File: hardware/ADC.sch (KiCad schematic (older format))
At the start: 21 parts, among them J4 691327310016, J5 691327310016

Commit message: Assigning footprints
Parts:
- C33, C34, C35, C36, C37, C38, C39, C40, C41, C42, C43, C44, C45, C46, C47, C48, C49, C50: renamed from C?; footprint (none) -> Capacitor_SMD:C_0603_1608Metric
- U1: renamed from U?; footprint QFP50P1200X1200X160-64N -> ADS8556IPM:QFP50P1200X1200X160-64N
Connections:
- net AVDD renamed 5V
- net BVDD renamed 3V3
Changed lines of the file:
@@
 AGND
 $Comp
-L antena:C C?
+L antena:C C33
 U 1 1 5E30FC12
 P 850 1150
-F 0 "C?" H 965 1196 50  0000 L CNN
+F 0 "C33" H 965 1196 50  0000 L CNN
 F 1 "100n" H 965 1105 50  0000 L CNN
-F 2 "" H 888 1000 50  0001 C CNN
+F 2 "Capacitor_SMD:C_0603_1608Metric" H 888 1000 50  0001 C CNN
 F 3 "~" H 850 1150 50  0001 C CNN
 	1    850  1150
@@
 AGND
 $Comp
-L antena:C C?
+L antena:C C38
 U 1 1 5E310EB0
 P 1300 1150
-F 0 "C?" H 1415 1196 50  0000 L CNN
+F 0 "C38" H 1415 1196 50  0000 L CNN
 F 1 "100n" H 1415 1105 50  0000 L CNN
-F 2 "" H 1338 1000 50  0001 C CNN
+F 2 "Capacitor_SMD:C_0603_1608Metric" H 1338 1000 50  0001 C CNN
 F 3 "~" H 1300 1150 50  0001 C CNN
 	1    1300 1150
@@
 AGND
 $Comp
-L antena:C C?
+L antena:C C41
 U 1 1 5E311894
 P 1700 1150
-F 0 "C?" H 1815 1196 50  0000 L CNN
+F 0 "C41" H 1815 1196 50  0000 L CNN
 F 1 "100n" H 1815 1105 50  0000 L CNN
-F 2 "" H 1738 1000 50  0001 C CNN
+F 2 "Capacitor_SMD:C_0603_1608Metric" H 1738 1000 50  0001 C CNN
 F 3 "~" H 1700 1150 50  0001 C CNN
 	1    1700 1150
@@
 AGND
 $Comp
-L antena:C C?
+L antena:C C46
 U 1 1 5E31189E
 P 2150 1150
-F 0 "C?" H 2265 1196 50  0000 L CNN
+F 0 "C46" H 2265 1196 50  0000 L CNN
 F 1 "100n" H 2265 1105 50  0000 L CNN
-F 2 "" H 2188 1000 50  0001 C CNN
+F 2 "Capacitor_SMD:C_0603_1608Metric" H 2188 1000 50  0001 C CNN
 F 3 "~" H 2150 1150 50  0001 C CNN
 	1    2150 1150
@@
 AGND
 $Comp
-L antena:C C?
+L antena:C C34
 U 1 1 5E3124A7
 P 850 2250
-F 0 "C?" H 965 2296 50  0000 L CNN
+F 0 "C34" H 965 2296 50  0000 L CNN
 F 1 "100n" H 965 2205 50  0000 L CNN
-F 2 "" H 888 2100 50  0001 C CNN
+F 2 "Capacitor_SMD:C_0603_1608Metric" H 888 2100 50  0001 C CNN
 F 3 "~" H 850 2250 50  0001 C CNN
 	1    850  2250
@@
 AGND
 $Comp
-L antena:C C?
+L antena:C C39
 U 1 1 5E3124B1
 P 1300 2250
-F 0 "C?" H 1415 2296 50  0000 L CNN
+F 0 "C39" H 1415 2296 50  0000 L CNN
 F 1 "100n" H 1415 2205 50  0000 L CNN
-F 2 "" H 1338 2100 50  0001 C CNN
+F 2 "Capacitor_SMD:C_0603_1608Metric" H 1338 2100 50  0001 C CNN
 F 3 "~" H 1300 2250 50  0001 C CNN
 	1    1300 2250
@@
 AGND
 $Comp
-L antena:C C?
+L antena:C C42
 U 1 1 5E3124BB
 P 1700 2250
-F 0 "C?" H 1815 2296 50  0000 L CNN
+F 0 "C42" H 1815 2296 50  0000 L CNN
 F 1 "100n" H 1815 2205 50  0000 L CNN
-F 2 "" H 1738 2100 50  0001 C CNN
+F 2 "Capacitor_SMD:C_0603_1608Metric" H 1738 2100 50  0001 C CNN
 F 3 "~" H 1700 2250 50  0001 C CNN
 	1    1700 2250
@@
 AGND
 $Comp
-L antena:C C?
+L antena:C C47
 U 1 1 5E3124C5
 P 2150 2250
-F 0 "C?" H 2265 2296 50  0000 L CNN
+F 0 "C47" H 2265 2296 50  0000 L CNN
 F 1 "100n" H 2265 2205 50  0000 L CNN
-F 2 "" H 2188 2100 50  0001 C CNN
+F 2 "Capacitor_SMD:C_0603_1608Metric" H 2188 2100 50  0001 C CNN
 F 3 "~" H 2150 2250 50  0001 C CNN
 	1    2150 2250
@@
 AGND
 $Comp
-L antena:C C?
+L antena:C C35
 U 1 1 5E31354C
 P 850 3450
-F 0 "C?" H 965 3496 50  0000 L CNN
+F 0 "C35" H 965 3496 50  0000 L CNN
 F 1 "100n" H 965 3405 50  0000 L CNN
-F 2 "" H 888 3300 50  0001 C CNN
+F 2 "Capacitor_SMD:C_0603_1608Metric" H 888 3300 50  0001 C CNN
 F 3 "~" H 850 3450 50  0001 C CNN
 	1    850  3450
@@
 	850  3600 850  3750
 $Comp
-L antena:C C?
+L antena:C C49
 U 1 1 5E315C6D
 P 7900 2450
-F 0 "C?" V 8152 2450 50  0000 C CNN
+F 0 "C49" V 8152 2450 50  0000 C CNN
 F 1 "10uF" V 8061 2450 50  0000 C CNN
-F 2 "" H 7938 2300 50  0001 C CNN
+F 2 "Capacitor_SMD:C_0603_1608Metric" H 7938 2300 50  0001 C CNN
 F 3 "~" H 7900 2450 50  0001 C CNN
 	1    7900 2450
@@
 $EndComp
 $Comp
-L antena:C C?
+L antena:C C50
 U 1 1 5E315D24
 P 7900 3750
-F 0 "C?" V 8152 3750 50  0000 C CNN
+F 0 "C50" V 8152 3750 50  0000 C CNN
 F 1 "10uF" V 8061 3750 50  0000 C CNN
-F 2 "" H 7938 3600 50  0001 C CNN
+F 2 "Capacitor_SMD:C_0603_1608Metric" H 7938 3600 50  0001 C CNN
 F 3 "~" H 7900 3750 50  0001 C CNN
 	1    7900 3750
@@
 $EndComp
 $Comp
-L antena:C C?
+L antena:C C48
 U 1 1 5E315E2D
 P 7600 3650
-F 0 "C?" V 7852 3650 50  0000 C CNN
+F 0 "C48" V 7852 3650 50  0000 C CNN
 F 1 "10uF" V 7761 3650 50  0000 C CNN
-F 2 "" H 7638 3500 50  0001 C CNN
+F 2 "Capacitor_SMD:C_0603_1608Metric" H 7638 3500 50  0001 C CNN
 F 3 "~" H 7600 3650 50  0001 C CNN
 	1    7600 3650
@@
 AGND
 $Comp
-L antena:C C?
+L antena:C C40
 U 1 1 5E31DDD7
 P 1300 3450
-F 0 "C?" H 1415 3496 50  0000 L CNN
+F 0 "C40" H 1415 3496 50  0000 L CNN
 F 1 "470n" H 1415 3405 50  0000 L CNN
-F 2 "" H 1338 3300 50  0001 C CNN
+F 2 "Capacitor_SMD:C_0603_1608Metric" H 1338 3300 50  0001 C CNN
 F 3 "~" H 1300 3450 50  0001 C CNN
 	1    1300 3450
@@
 AGND
 $Comp
-L antena:C C?
+L antena:C C44
 U 1 1 5E31FB8F
 P 1800 3450
-F 0 "C?" H 1915 3496 50  0000 L CNN
+F 0 "C44" H 1915 3496 50  0000 L CNN
 F 1 "1uF" H 1915 3405 50  0000 L CNN
-F 2 "" H 1838 3300 50  0001 C CNN
+F 2 "Capacitor_SMD:C_0603_1608Metric" H 1838 3300 50  0001 C CNN
 F 3 "~" H 1800 3450 50  0001 C CNN
 	1    1800 3450
@@
 	7950 5050 8100 5050
 $Comp
-L antena:C C?
+L antena:C C37
 U 1 1 5E327225
 P 1250 4800
-F 0 "C?" H 1365 4846 50  0000 L CNN
+F 0 "C37" H 1365 4846 50  0000 L CNN
 F 1 "10uF" H 1365 4755 50  0000 L CNN
-F 2 "" H 1288 4650 50  0001 C CNN
+F 2 "Capacitor_SMD:C_0603_1608Metric" H 1288 4650 50  0001 C CNN
 F 3 "~" H 1250 4800 50  0001 C CNN
 	1    1250 4800
@@
 $EndComp
 $Comp
-L antena:C C?
+L antena:C C45
 U 1 1 5E327301
 P 2100 4800
-F 0 "C?" H 2215 4846 50  0000 L CNN
+F 0 "C45" H 2215 4846 50  0000 L CNN
 F 1 "10uF" H 2215 4755 50  0000 L CNN
-F 2 "" H 2138 4650 50  0001 C CNN
+F 2 "Capacitor_SMD:C_0603_1608Metric" H 2138 4650 50  0001 C CNN
 F 3 "~" H 2100 4800 50  0001 C CNN
 	1    2100 4800
@@
 $EndComp
 $Comp
-L antena:C C?
+L antena:C C36
 U 1 1 5E327389
 P 850 4800
-F 0 "C?" H 965 4846 50  0000 L CNN
+F 0 "C36" H 965 4846 50  0000 L CNN
 F 1 "100n" H 965 4755 50  0000 L CNN
-F 2 "" H 888 4650 50  0001 C CNN
+F 2 "Capacitor_SMD:C_0603_1608Metric" H 888 4650 50  0001 C CNN
 F 3 "~" H 850 4800 50  0001 C CNN
 	1    850  4800
@@
 $EndComp
 $Comp
-L antena:C C?
+L antena:C C43
 U 1 1 5E32742F
 P 1700 4800
-F 0 "C?" H 1815 4846 50  0000 L CNN
+F 0 "C43" H 1815 4846 50  0000 L CNN
 F 1 "100n" H 1815 4755 50  0000 L CNN
-F 2 "" H 1738 4650 50  0001 C CNN
+F 2 "Capacitor_SMD:C_0603_1608Metric" H 1738 4650 50  0001 C CNN
 F 3 "~" H 1700 4800 50  0001 C CNN
 	1    1700 4800
@@
 	7500 3850 8150 3850
 $Comp
-L ADS8556IPM:ADS8556IPM U?
+L ADS8556IPM:ADS8556IPM U1
 U 1 1 5E473826
 P 9350 3550
-F 0 "U?" H 9350 6320 50  0000 C CNN
+F 0 "U1" H 9350 6320 50  0000 C CNN
 F 1 "ADS8556IPM" H 9350 6229 50  0000 C CNN
-F 2 "QFP50P1200X1200X160-64N" H 9350 3550 50  0001 L BNN
+F 2 "ADS8556IPM:QFP50P1200X1200X160-64N" H 9350 3550 50  0001 L BNN
 F 3 "QFP-64" H 9350 3550 50  0001 L BNN
 F 4 "TEXAS INSTRUMENTS" H 9350 3550 50  0001 L BNN "Field4"
@@
 Wire Wire Line
 	4000 2750 4100 2750
+Text GLabel 2700 3750 3    50   Input ~ 0
+AGND
+Text GLabel 2700 3600 1    50   Input ~ 0
+GND
+Wire Wire Line
+	2700 3600 2700 3750
+Text GLabel 2950 3750 3    50   Input ~ 0
+BVDD
+Text GLabel 2950 3600 1    50   Input ~ 0
+3V3
+Wire Wire Line
+	2950 3600 2950 3750
+Text GLabel 3150 3600 1    50   Input ~ 0
+AVDD
+Text GLabel 3150 3750 3    50   Input ~ 0
+5V
+Wire Wire Line
+	3150 3600 3150 3750
 $EndSCHEMATC

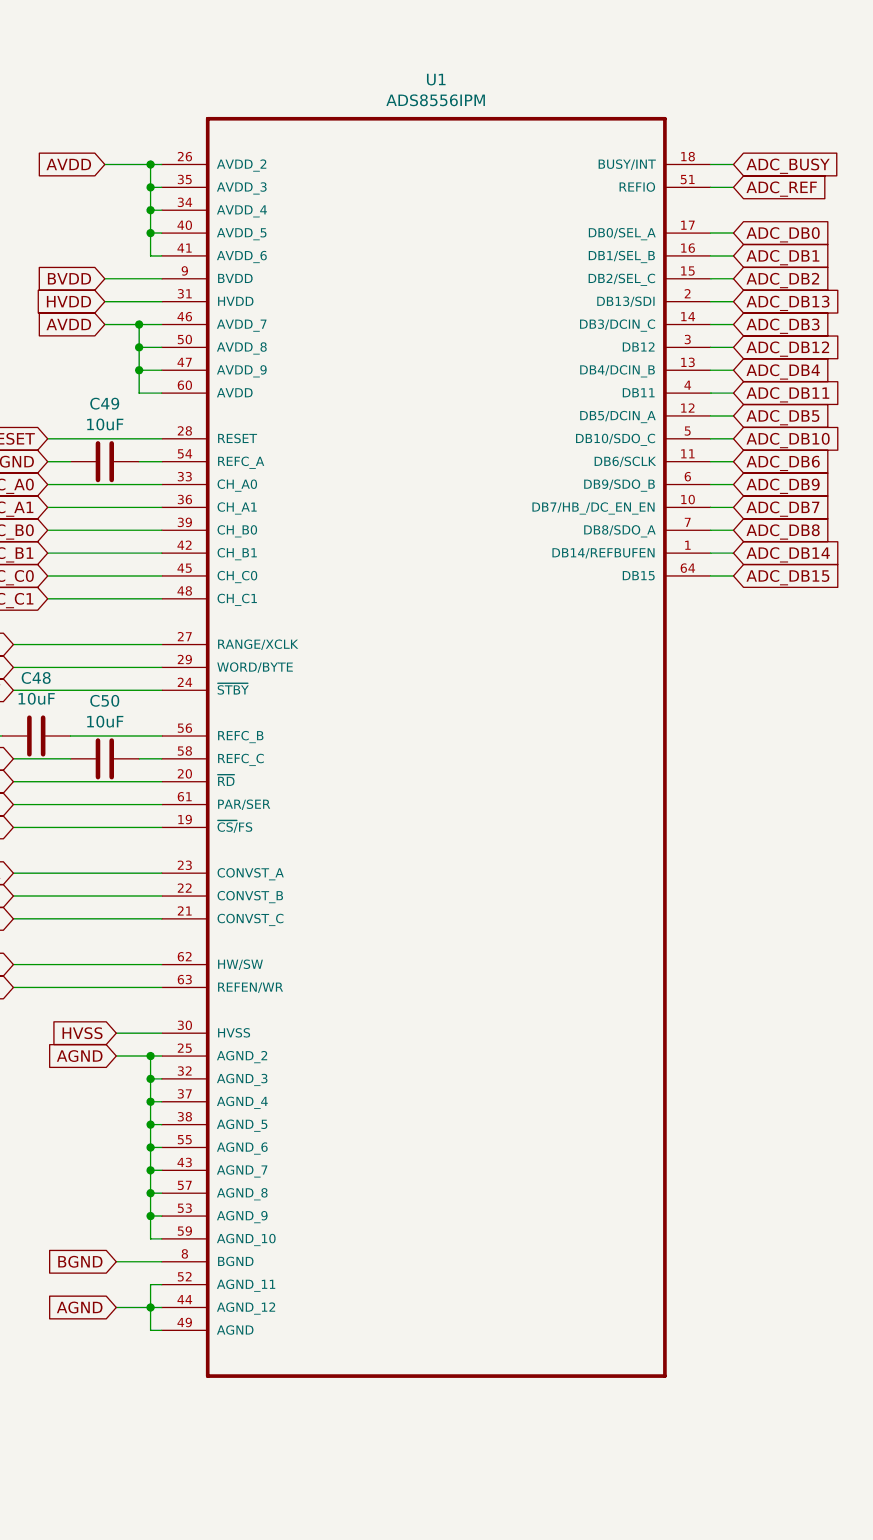
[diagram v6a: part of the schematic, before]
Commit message: Adding chip power down fix - removing ADS8556 chip
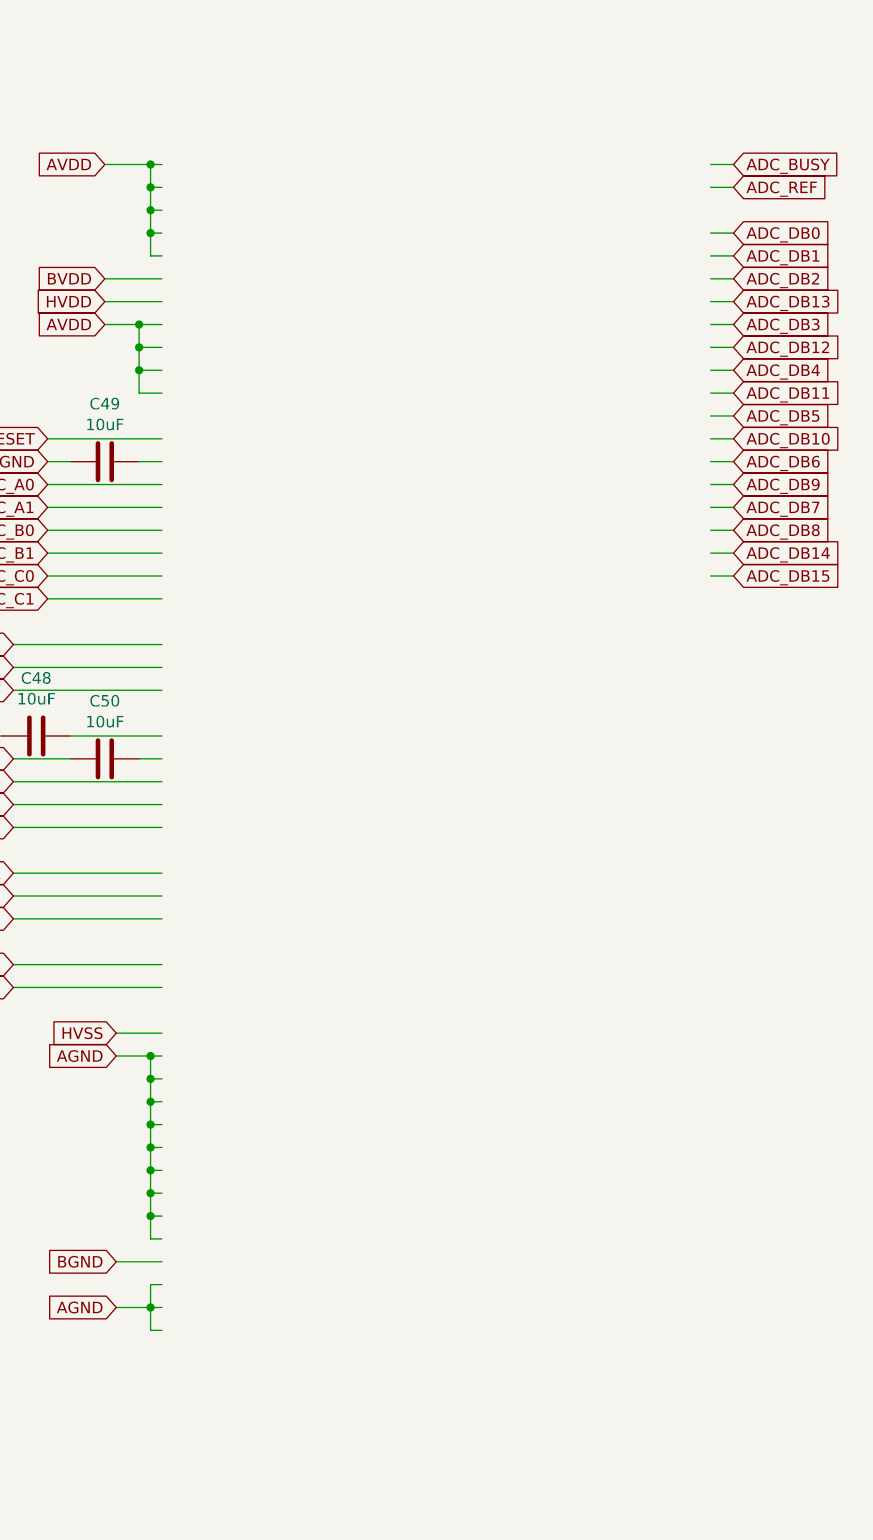
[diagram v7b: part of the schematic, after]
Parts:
- removed U1: ADS8556IPM, ADS8556IPM:QFP50P1200X1200X160-64N, symbol ADS8556IPM:ADS8556IPM
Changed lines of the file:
@@
 Wire Wire Line
 	7500 3850 8150 3850
-$Comp
-L ADS8556IPM:ADS8556IPM U1
-U 1 1 5E473826
-P 9350 3550
-F 0 "U1" H 9350 6320 50  0000 C CNN
-F 1 "ADS8556IPM" H 9350 6229 50  0000 C CNN
-F 2 "ADS8556IPM:QFP50P1200X1200X160-64N" H 9350 3550 50  0001 L BNN
-F 3 "QFP-64" H 9350 3550 50  0001 L BNN
-F 4 "TEXAS INSTRUMENTS" H 9350 3550 50  0001 L BNN "Field4"
-F 5 "26R5213" H 9350 3550 50  0001 L BNN "Field5"
-F 6 "1762983" H 9350 3550 50  0001 L BNN "Field6"
-F 7 "ADS8556IPM" H 9350 3550 50  0001 L BNN "Field7"
-	1    9350 3550
-	1    0    0    -1
-$EndComp
 Wire Notes Line
 	750  600  2500 600

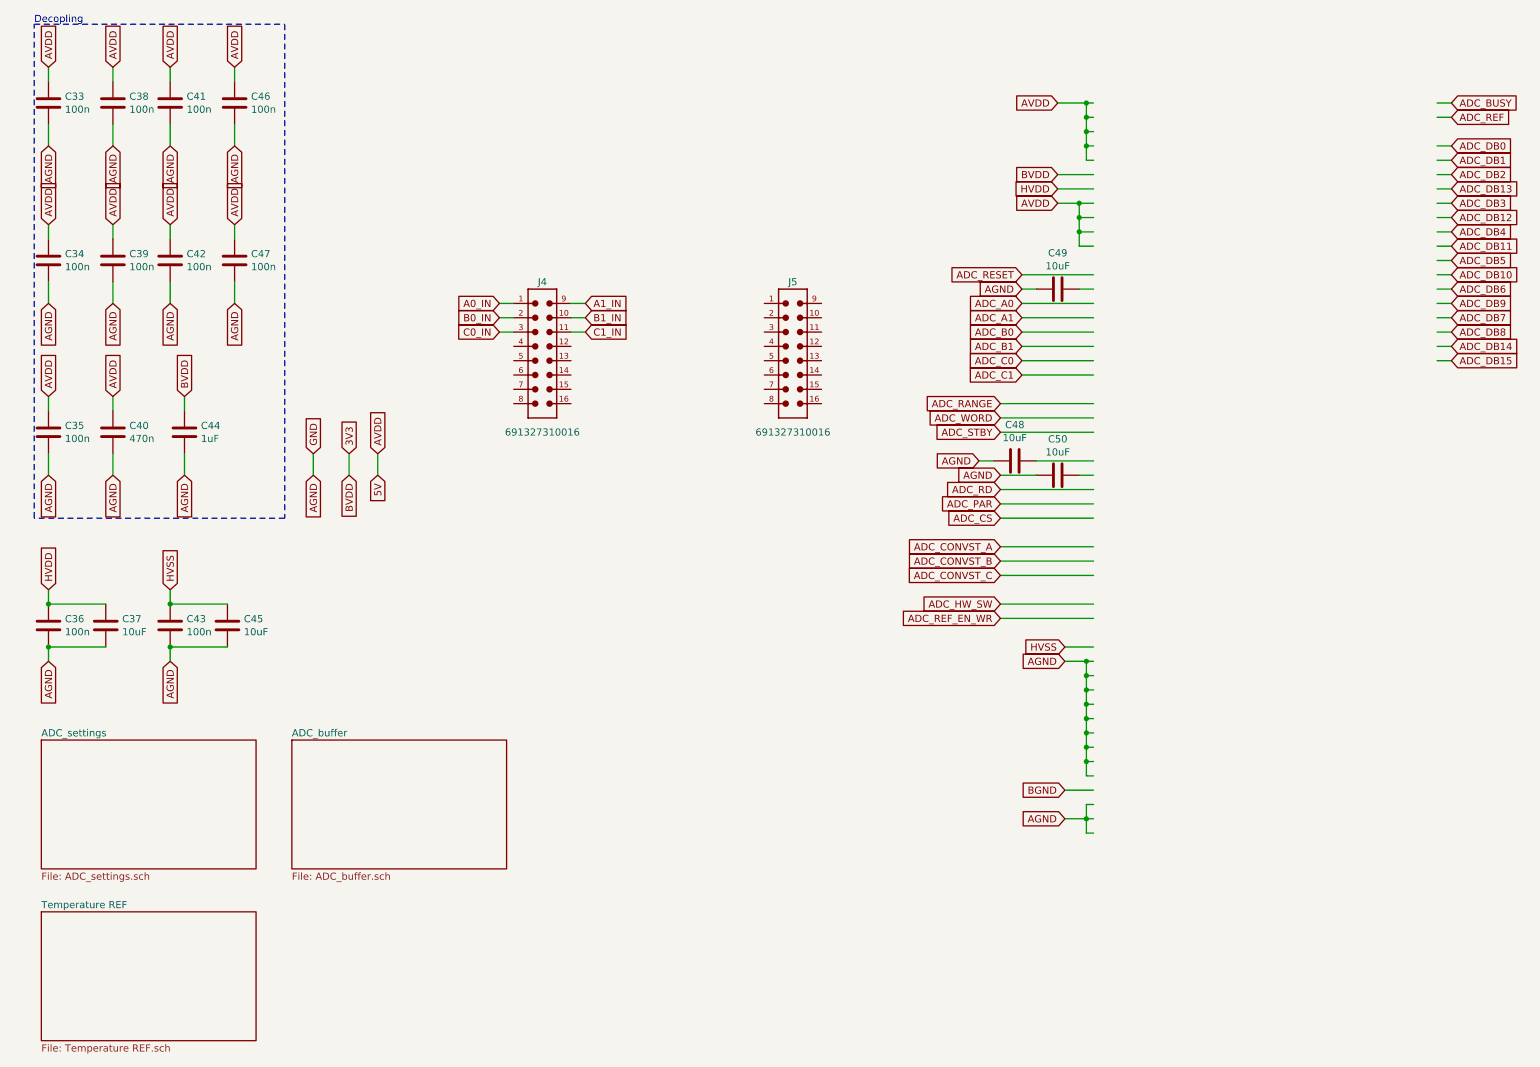
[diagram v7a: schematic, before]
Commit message: Adding ads8586s to shematics
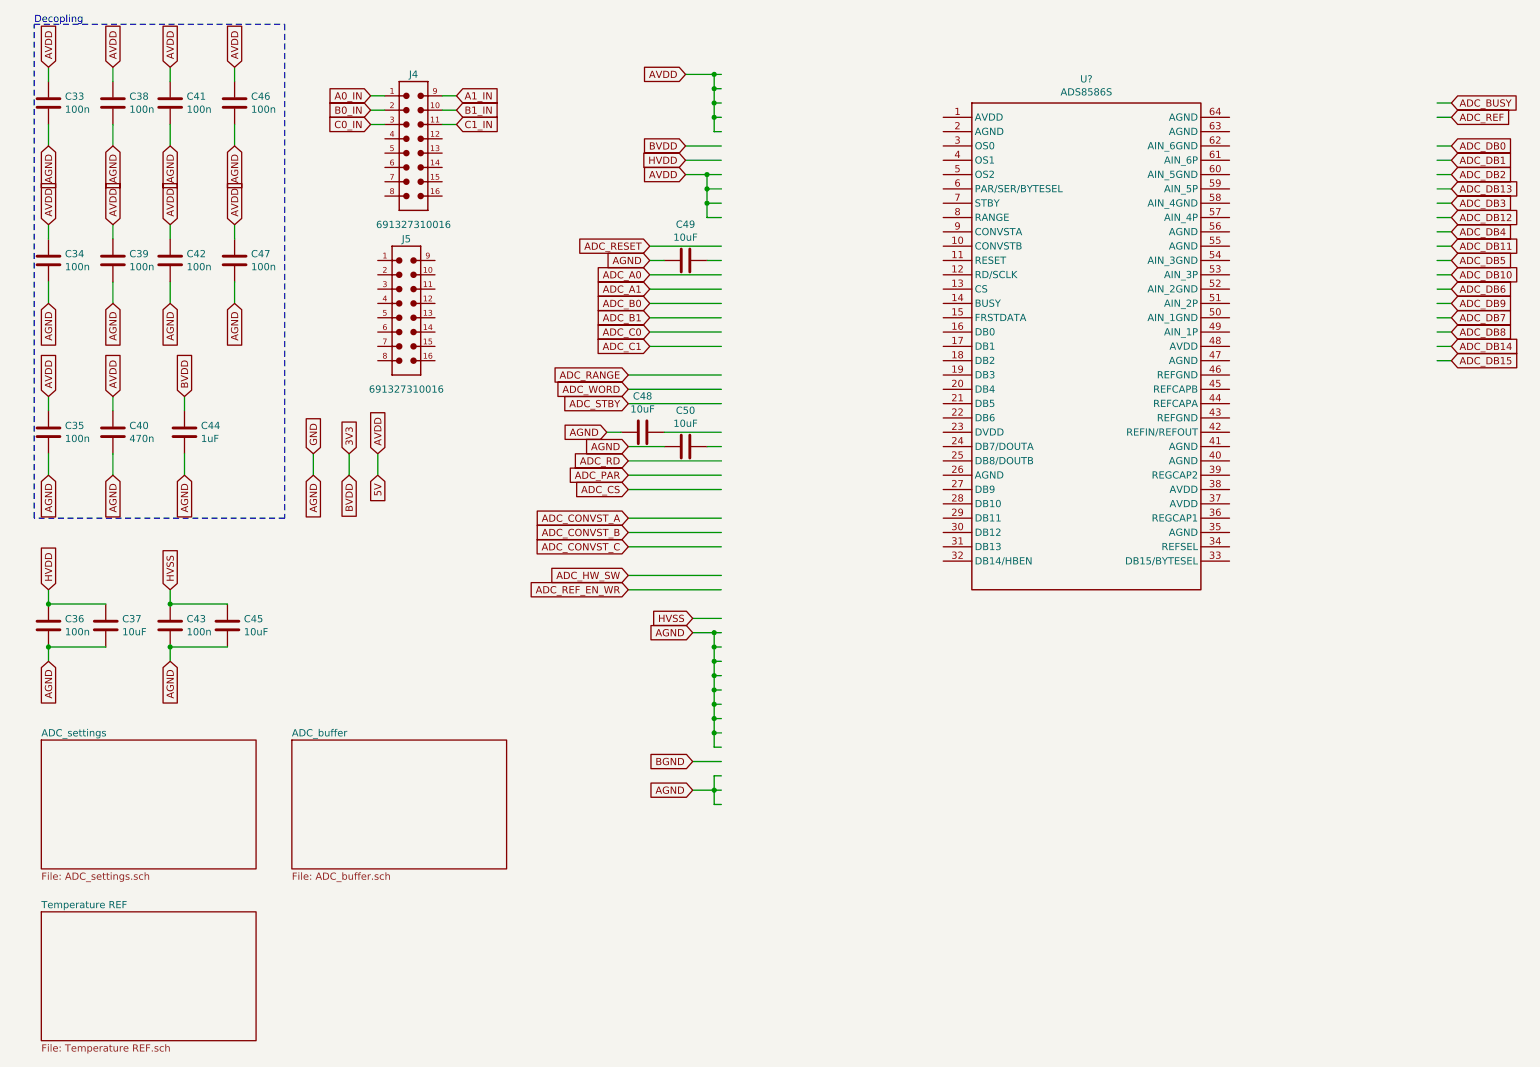
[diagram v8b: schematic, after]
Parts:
- added U?: ADS8586S, symbol ads8586s:ADS8586S
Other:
- moved on the sheet: C48, C49, C50, J4, J5
